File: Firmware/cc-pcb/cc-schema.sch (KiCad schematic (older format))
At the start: 7 parts

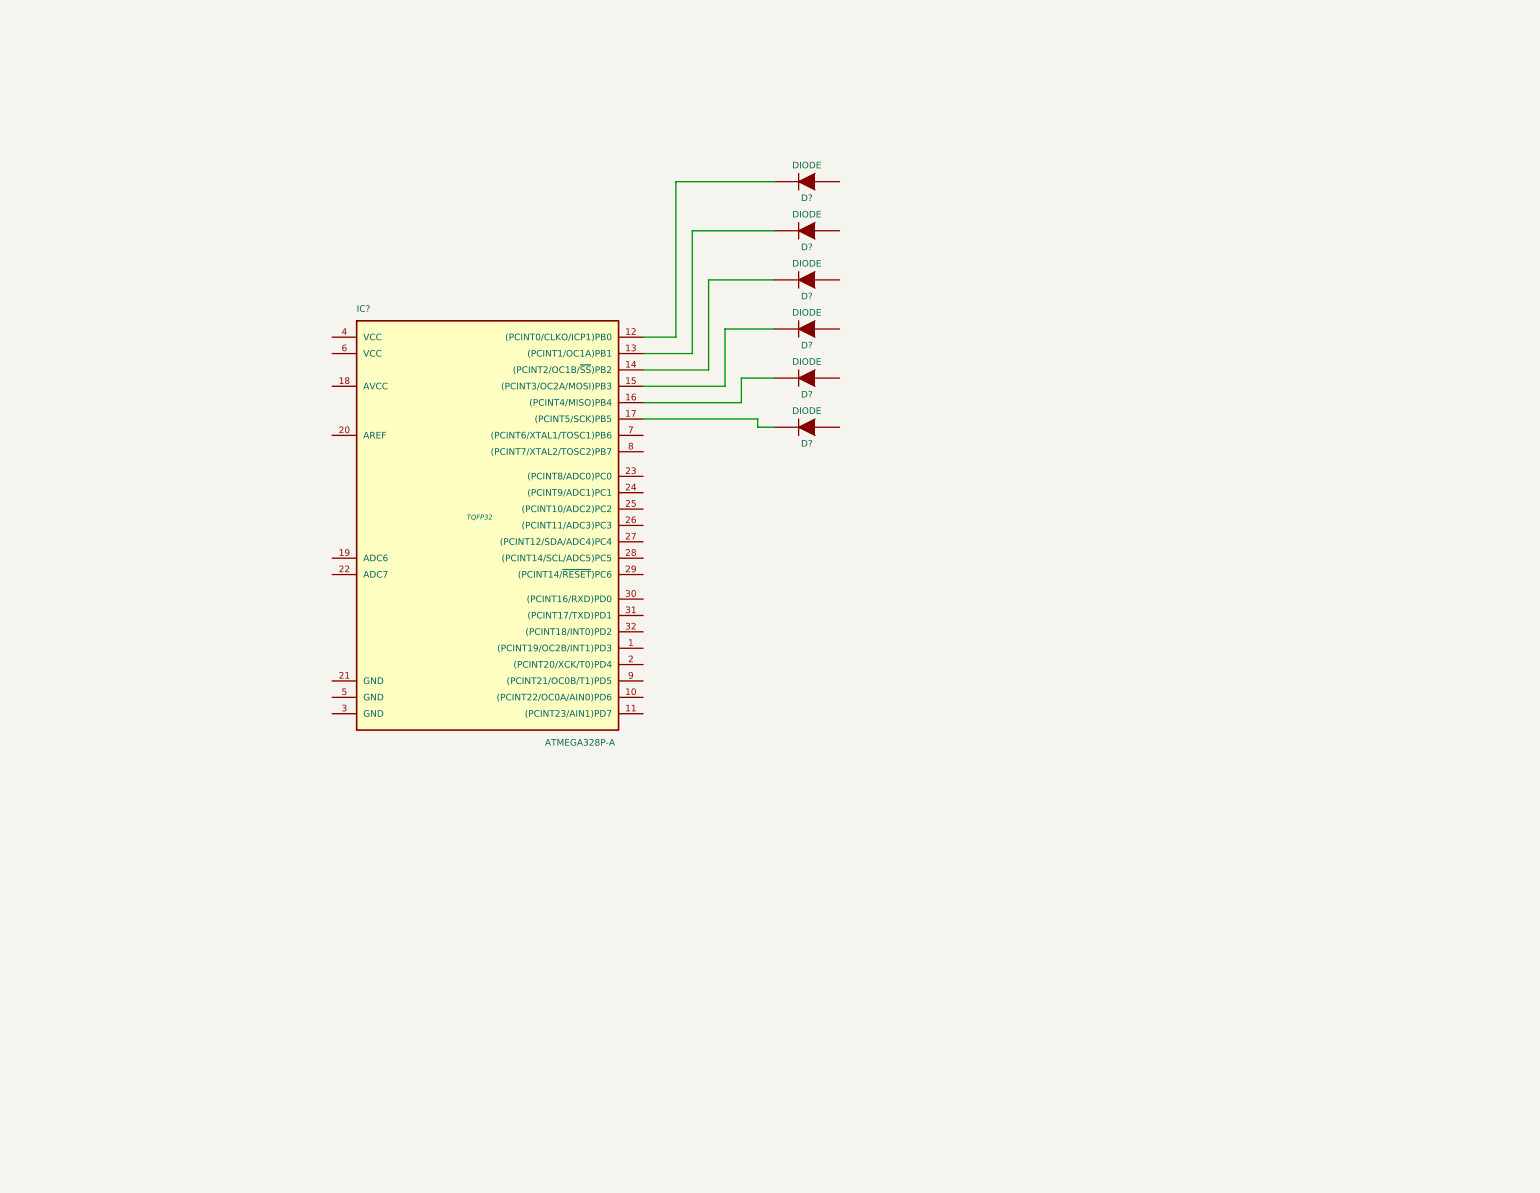
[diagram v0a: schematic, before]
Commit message: Edited schema, added 36 switches and other stuff
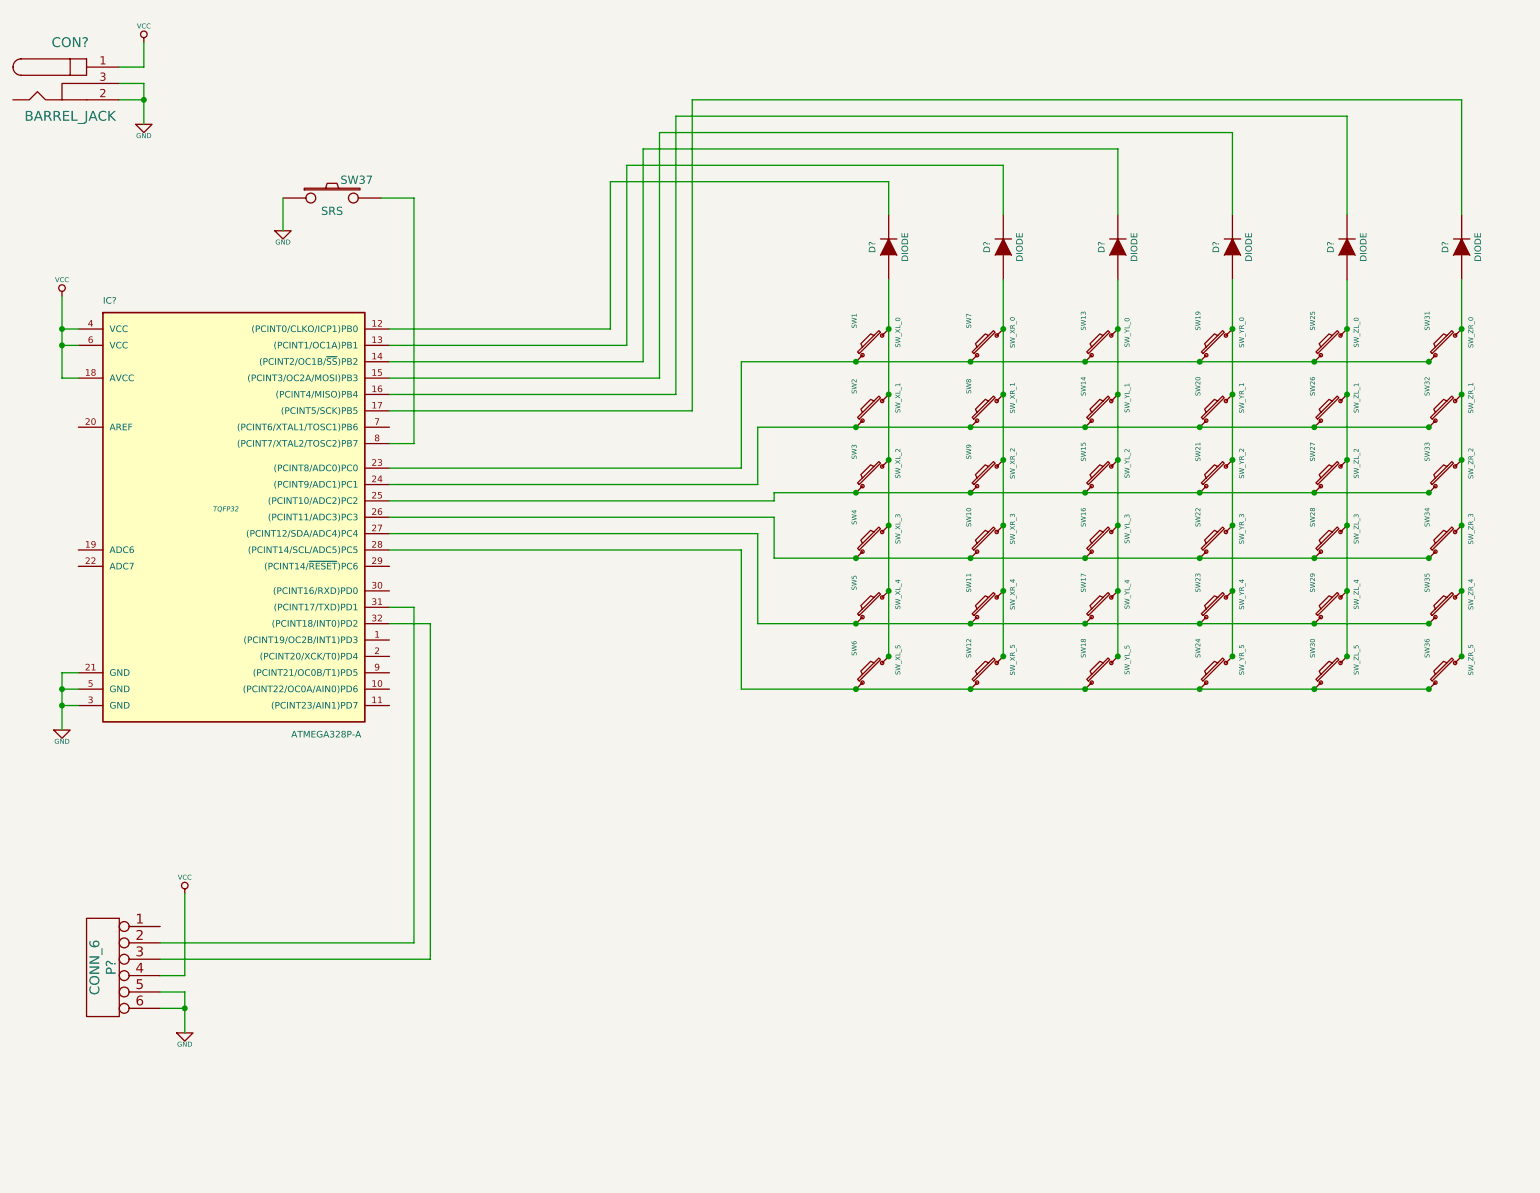
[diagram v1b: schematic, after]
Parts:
- added CON?: BARREL_JACK, symbol BARREL_JACK
- added P?: CONN_6, symbol CONN_6
- added SW1: SW_XL_0, ~, symbol SW_PUSH_SMALL
- added SW10: SW_XR_3, ~, symbol SW_PUSH_SMALL
- added SW11: SW_XR_4, ~, symbol SW_PUSH_SMALL
- added SW12: SW_XR_5, ~, symbol SW_PUSH_SMALL
- added SW13: SW_YL_0, ~, symbol SW_PUSH_SMALL
- added SW14: SW_YL_1, ~, symbol SW_PUSH_SMALL
- added SW15: SW_YL_2, ~, symbol SW_PUSH_SMALL
- added SW16: SW_YL_3, ~, symbol SW_PUSH_SMALL
- added SW17: SW_YL_4, ~, symbol SW_PUSH_SMALL
- added SW18: SW_YL_5, ~, symbol SW_PUSH_SMALL
- added SW19: SW_YR_0, ~, symbol SW_PUSH_SMALL
- added SW2: SW_XL_1, ~, symbol SW_PUSH_SMALL
- added SW20: SW_YR_1, ~, symbol SW_PUSH_SMALL
- added SW21: SW_YR_2, ~, symbol SW_PUSH_SMALL
- added SW22: SW_YR_3, ~, symbol SW_PUSH_SMALL
- added SW23: SW_YR_4, ~, symbol SW_PUSH_SMALL
- added SW24: SW_YR_5, ~, symbol SW_PUSH_SMALL
- added SW25: SW_ZL_0, ~, symbol SW_PUSH_SMALL
- added SW26: SW_ZL_1, ~, symbol SW_PUSH_SMALL
- added SW27: SW_ZL_2, ~, symbol SW_PUSH_SMALL
- added SW28: SW_ZL_3, ~, symbol SW_PUSH_SMALL
- added SW29: SW_ZL_4, ~, symbol SW_PUSH_SMALL
- added SW3: SW_XL_2, ~, symbol SW_PUSH_SMALL
- added SW30: SW_ZL_5, ~, symbol SW_PUSH_SMALL
- added SW31: SW_ZR_0, ~, symbol SW_PUSH_SMALL
- added SW32: SW_ZR_1, ~, symbol SW_PUSH_SMALL
- added SW33: SW_ZR_2, ~, symbol SW_PUSH_SMALL
- added SW34: SW_ZR_3, ~, symbol SW_PUSH_SMALL
- added SW35: SW_ZR_4, ~, symbol SW_PUSH_SMALL
- added SW36: SW_ZR_5, ~, symbol SW_PUSH_SMALL
- added SW37: SRS, ~, symbol SW_PUSH
- added SW4: SW_XL_3, ~, symbol SW_PUSH_SMALL
- added SW5: SW_XL_4, ~, symbol SW_PUSH_SMALL
- added SW6: SW_XL_5, ~, symbol SW_PUSH_SMALL
- added SW7: SW_XR_0, ~, symbol SW_PUSH_SMALL
- added SW8: SW_XR_1, ~, symbol SW_PUSH_SMALL
- added SW9: SW_XR_2, ~, symbol SW_PUSH_SMALL
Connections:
- net VCC: now reaches IC?.18 (AVCC)
- net VCC: now also IC?.4 (VCC), IC?.6 (VCC), CON?.1, P?.4
- net GND: now reaches IC?.21 (GND)
- net GND: now also IC?.3 (GND), IC?.5 (GND), CON?.2, CON?.3, P?.5, P?.6, SW37.1
- net at IC?.23 ((PCINT8/ADC0)PC0): now also SW1.1, SW13.1, SW19.1, SW25.1, SW31.1, SW7.1
- net at IC?.24 ((PCINT9/ADC1)PC1): now also SW14.1, SW2.1, SW20.1, SW26.1, SW32.1, SW8.1
- net at IC?.25 ((PCINT10/ADC2)PC2): now also SW15.1, SW21.1, SW27.1, SW3.1, SW33.1, SW9.1
- net at IC?.26 ((PCINT11/ADC3)PC3): now also SW10.1, SW16.1, SW22.1, SW28.1, SW34.1, SW4.1
- net at IC?.27 ((PCINT12/SDA/ADC4)PC4): now also SW11.1, SW17.1, SW23.1, SW29.1, SW35.1, SW5.1
- net at IC?.28 ((PCINT14/SCL/ADC5)PC5): now also SW12.1, SW18.1, SW24.1, SW30.1, SW36.1, SW6.1
- net at IC?.31 ((PCINT17/TXD)PD1): now also P?.2
- net at IC?.32 ((PCINT18/INT0)PD2): now also P?.3
- net at IC?.8 ((PCINT7/XTAL2/TOSC2)PB7): now also SW37.2
- net at D?.1 (A): now also SW1.2, SW2.2, SW3.2, SW4.2, SW5.2, SW6.2
- net at D?.1 (A): now also SW10.2, SW11.2, SW12.2, SW7.2, SW8.2, SW9.2
- net at D?.1 (A): now also SW13.2, SW14.2, SW15.2, SW16.2, SW17.2, SW18.2
- net at D?.1 (A): now also SW19.2, SW20.2, SW21.2, SW22.2, SW23.2, SW24.2
- net at D?.1 (A): now also SW25.2, SW26.2, SW27.2, SW28.2, SW29.2, SW30.2
- net at D?.1 (A): now also SW31.2, SW32.2, SW33.2, SW34.2, SW35.2, SW36.2
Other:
- moved on the sheet: D?, IC?

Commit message: Edited schema, added connectors, reset, power capacitor
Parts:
- added C1: 10uF, ~, symbol CP1
- added C2: 0.1uF, ~, symbol C
- added P?: CONN_6, symbol CONN_6
- added R1: 10k, ~, symbol R
- gave numbers to parts that had none: 6
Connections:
- net GND: now also SW37.2, C1.2, P?.6; no longer SW37.1
- net VCC: now also IC?.20 (AREF), C1.1, P?.2, R1.1
- net at D4.2 (K), IC?.15 ((PCINT3/OC2A/MOSI)PB3): now also P?.4
- net at D5.2 (K), IC?.16 ((PCINT4/MISO)PB4): now also P?.1
- net at D6.2 (K), IC?.17 ((PCINT5/SCK)PB5): now also P?.3
- net at IC?.29 ((PCINT14/~RESET~)PC6): now also C2.1, P?.5, R1.2
- net at IC?.8 ((PCINT7/XTAL2/TOSC2)PB7): now also SW37.1; no longer SW37.2
- net at P?.1: now also C2.2
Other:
- moved on the sheet: P?, SW37

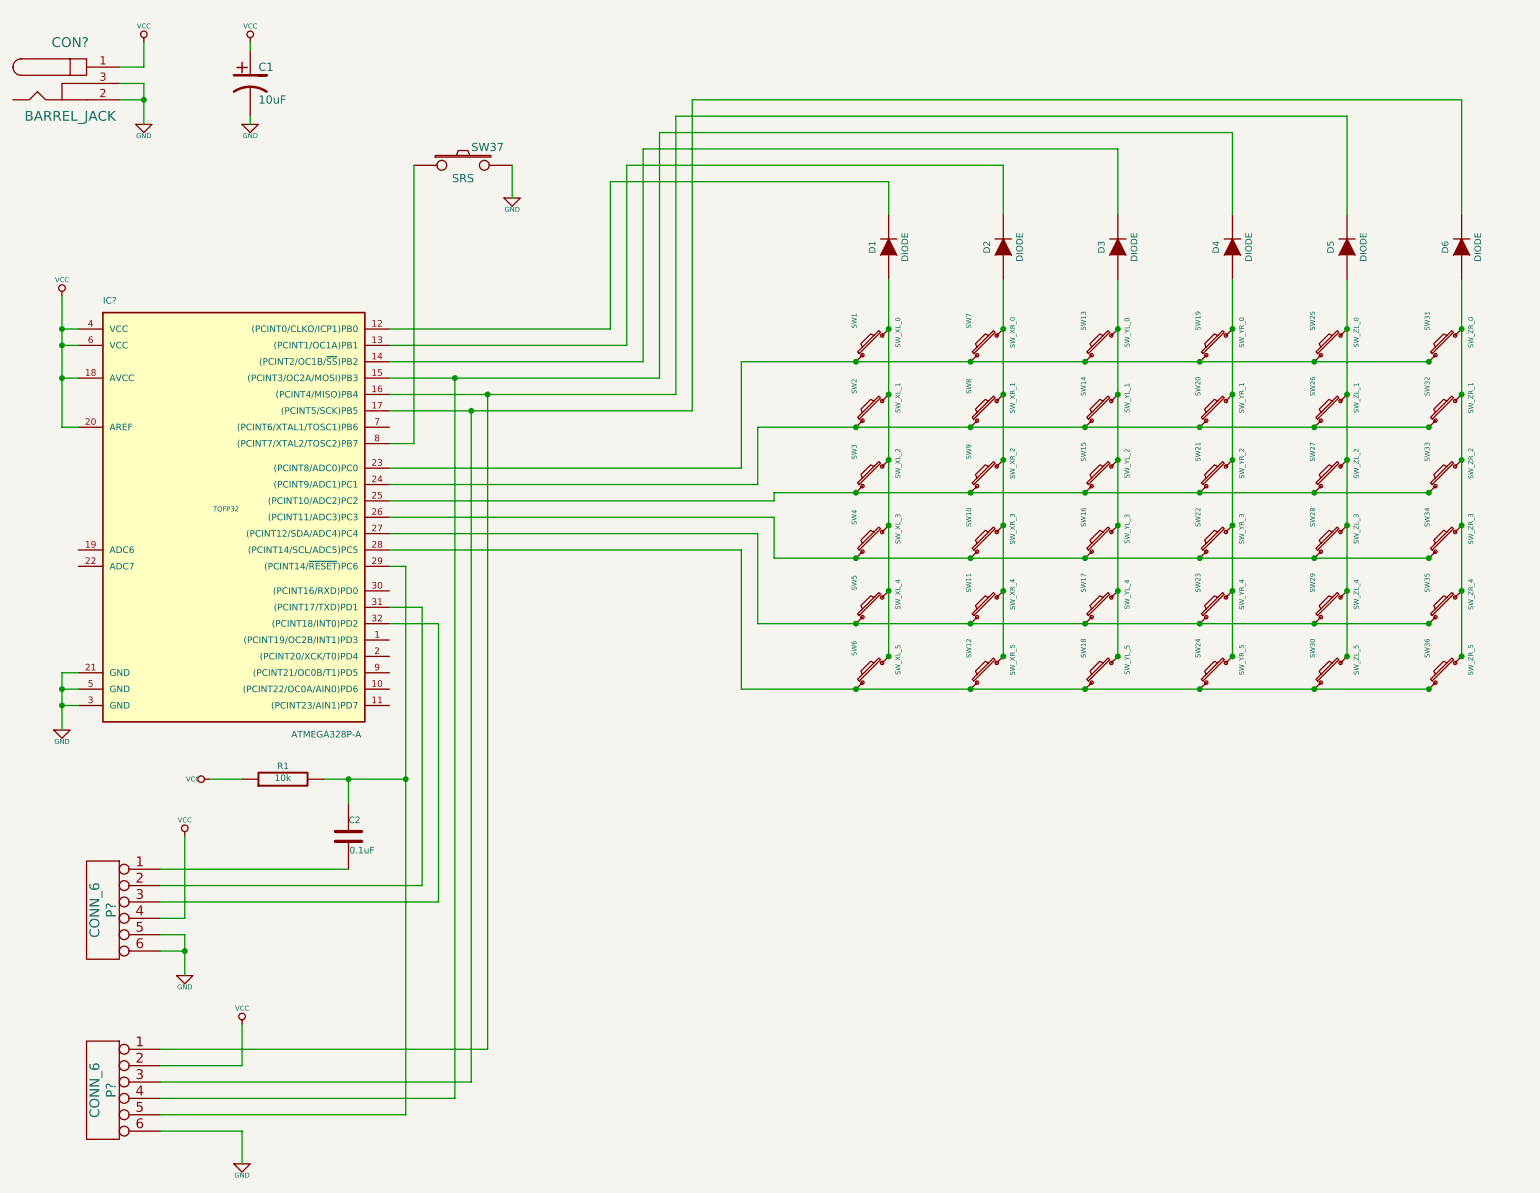
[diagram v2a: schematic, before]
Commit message: Edited schema, added ws2812b's
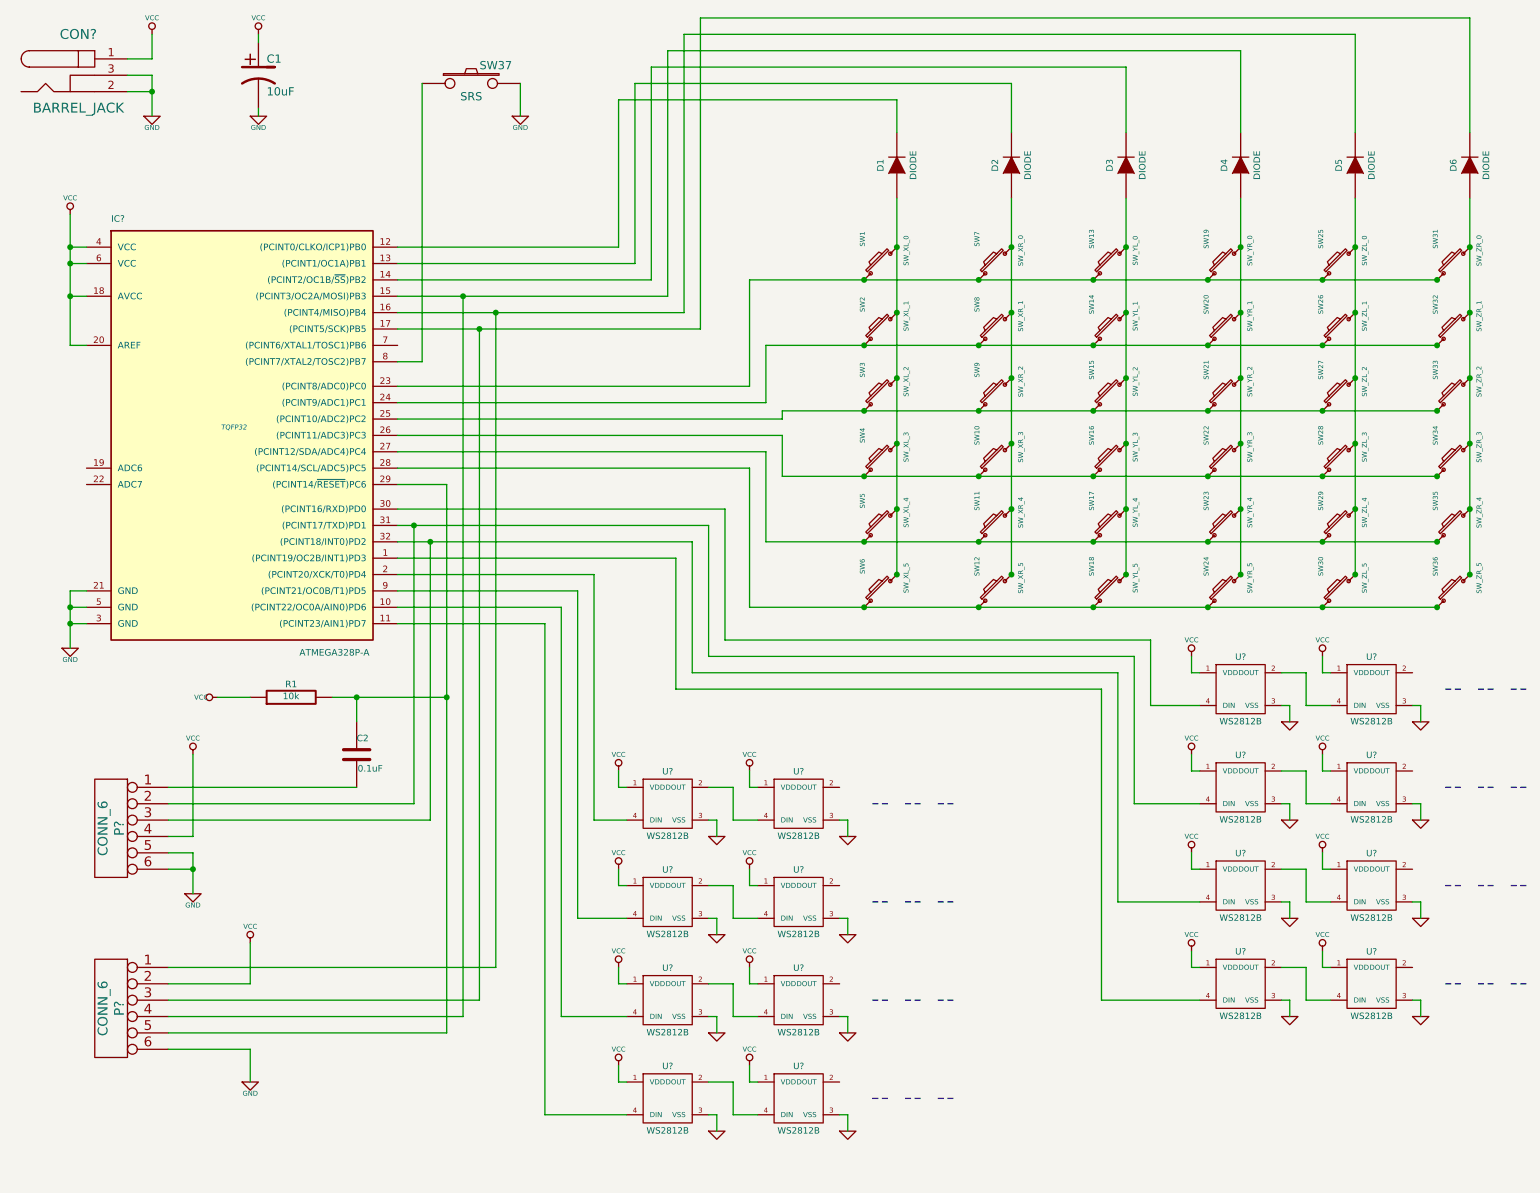
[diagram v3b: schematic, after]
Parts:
- added U? (x16): WS2812B, symbol WS2812B
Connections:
- net GND: now also U?.3 (VSS), U?.3 (VSS), U?.3 (VSS), U?.3 (VSS), U?.3 (VSS), U?.3 (VSS), U?.3 (VSS), U?.3 (VSS), U?.3 (VSS), U?.3 (VSS), U?.3 (VSS), U?.3 (VSS), U?.3 (VSS), U?.3 (VSS), U?.3 (VSS), U?.3 (VSS)
- net VCC: now also U?.1 (VDD), U?.1 (VDD), U?.1 (VDD), U?.1 (VDD), U?.1 (VDD), U?.1 (VDD), U?.1 (VDD), U?.1 (VDD), U?.1 (VDD), U?.1 (VDD), U?.1 (VDD), U?.1 (VDD), U?.1 (VDD), U?.1 (VDD), U?.1 (VDD), U?.1 (VDD)
- net at IC?.1 ((PCINT19/OC2B/INT1)PD3): now also U?.4 (DIN)
- net at IC?.10 ((PCINT22/OC0A/AIN0)PD6): now also U?.4 (DIN)
- net at IC?.11 ((PCINT23/AIN1)PD7): now also U?.4 (DIN)
- net at IC?.2 ((PCINT20/XCK/T0)PD4): now also U?.4 (DIN)
- net at IC?.30 ((PCINT16/RXD)PD0): now also U?.4 (DIN)
- net at IC?.31 ((PCINT17/TXD)PD1), P?.2: now also U?.4 (DIN)
- net at IC?.32 ((PCINT18/INT0)PD2), P?.3: now also U?.4 (DIN)
- net at IC?.9 ((PCINT21/OC0B/T1)PD5): now also U?.4 (DIN)
- new net: U?.2 (DOUT), U?.4 (DIN) (x8)
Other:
- moved on the sheet: C1, C2, CON?, D1, D2, D3, D4, D5, D6, IC?, P?, R1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
